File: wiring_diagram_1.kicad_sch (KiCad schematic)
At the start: 0 parts

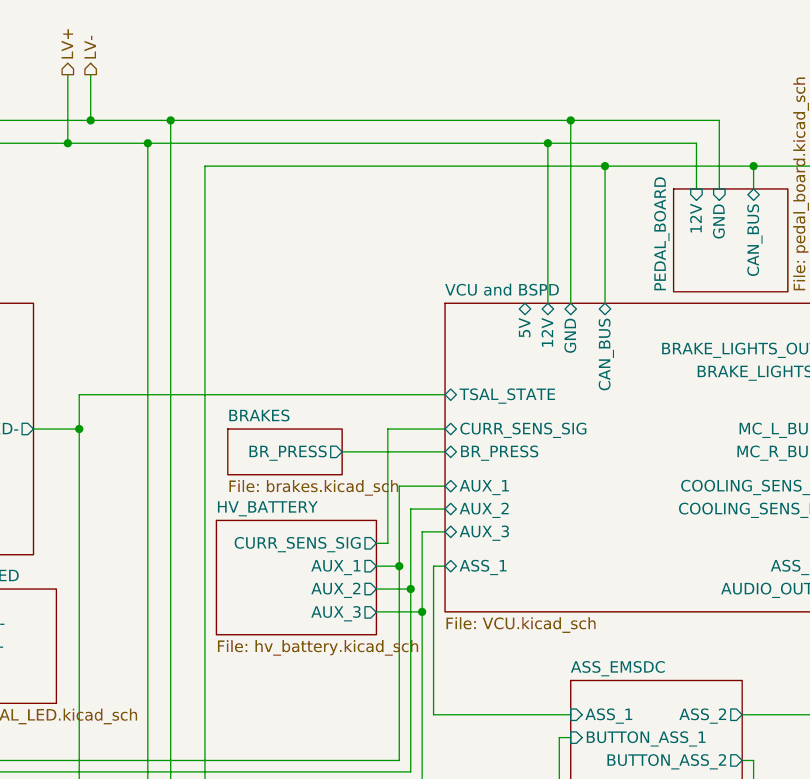
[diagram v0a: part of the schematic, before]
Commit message: Add bms
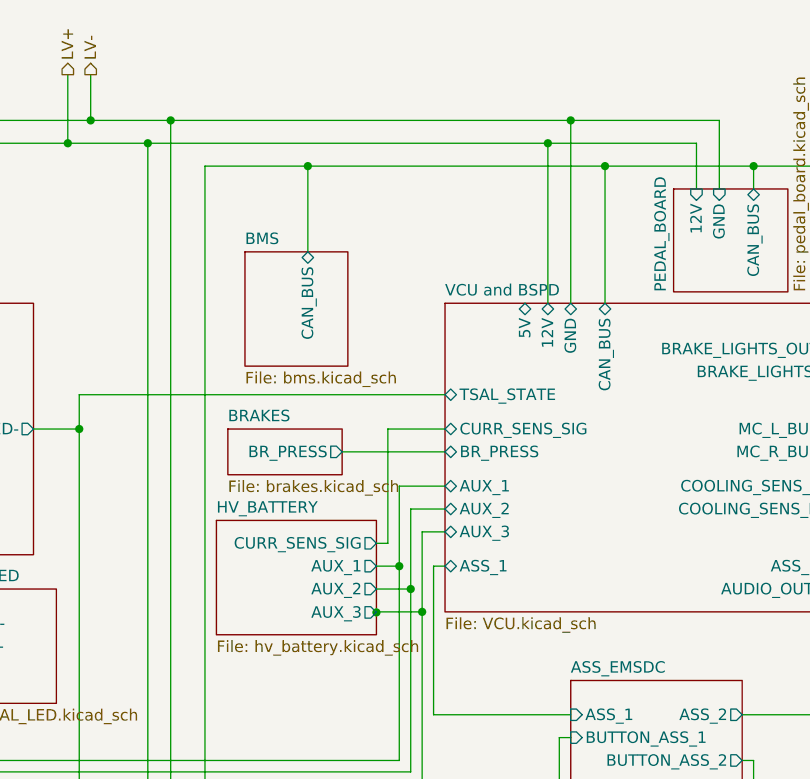
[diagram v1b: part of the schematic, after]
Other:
- added sheet BMS (bms.kicad_sch)
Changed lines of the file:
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@@
     (comment 2 "Electronics team")
   )
+  (junction (at 165.1 52.07) (diameter 0) (color 0 0 0 0)
+  )
   (junction (at 149.86 46.99) (diameter 0) (color 0 0 0 0)
   )
@@
   (junction (at 194.31 46.99) (diameter 0) (color 0 0 0 0)
   )
+  (junction (at 172.72 101.6584) (diameter 0) (color 0 0 0 0)
+  )
   (junction (at 245.11 100.33) (diameter 0) (color 0 0 0 0)
   )
@@
     (stroke (width 0) (type default) (color 0 0 0 0))
   )
-  (wire (pts (xy 153.67 52.07) (xy 198.12 52.07))
+  (wire (pts (xy 153.67 52.07) (xy 165.1 52.07))
     (stroke (width 0) (type default) (color 0 0 0 0))
   )
@@
     (stroke (width 0) (type default) (color 0 0 0 0))
   )
+  (wire (pts (xy 165.1 52.07) (xy 198.12 52.07))
+    (stroke (width 0) (type default) (color 0 0 0 0))
+  )
   (wire (pts (xy 140.97 46.99) (xy 140.97 41.91))
     (stroke (width 0) (type default) (color 0 0 0 0))
@@
   )
   (wire (pts (xy 245.11 52.07) (xy 245.11 81.28))
+    (stroke (width 0) (type default) (color 0 0 0 0))
+  )
+  (wire (pts (xy 165.1 52.07) (xy 165.1 61.595))
     (stroke (width 0) (type default) (color 0 0 0 0))
   )
@@
   (hierarchical_label "LV-" (shape output) (at 140.97 41.91 90)
     (effects (font (size 1.27 1.27)) (justify left))
+  )
+  (sheet (at 158.115 61.595) (size 11.43 12.7) (fields_autoplaced)
+    (stroke (width 0.1524) (type solid) (color 0 0 0 0))
+    (fill (color 255 255 194 1.0000))
+    (property "Sheet name" "BMS" (id 0) (at 158.115 60.8834 0)
+      (effects (font (size 1.27 1.27)) (justify left bottom))
+    )
+    (property "Sheet file" "bms.kicad_sch" (id 1) (at 158.115 74.8796 0)
+      (effects (font (size 1.27 1.27)) (justify left top))
+    )
+    (pin "CAN_BUS" tri_state (at 165.1 61.595 90)
+      (effects (font (size 1.27 1.27)) (justify right))
+    )
   )
   (sheet (at 194.31 109.22) (size 19.05 11.43) (fields_autoplaced)
@@
     (path "/2ee454ec-f665-4144-bdd4-187d67e3c54f" (page "13"))
     (path "/3e919e67-6089-4e71-bfb6-348566d23397" (page "14"))
+    (path "/004b7456-c25a-480f-88f6-723c1bcd9939" (page "15"))
   )
 )
